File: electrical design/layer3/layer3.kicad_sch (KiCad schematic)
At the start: 6 parts, among them U1 TEENSY4.0

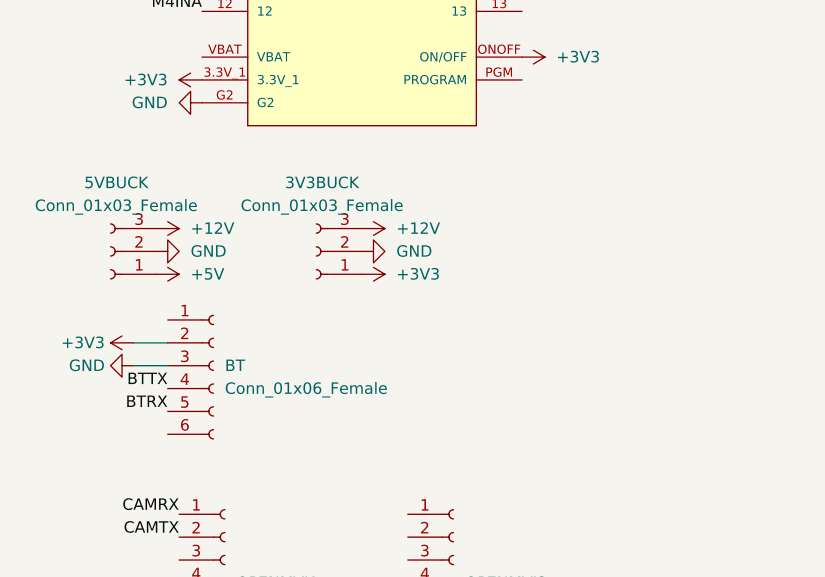
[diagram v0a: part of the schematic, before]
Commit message: add support for bldc esc
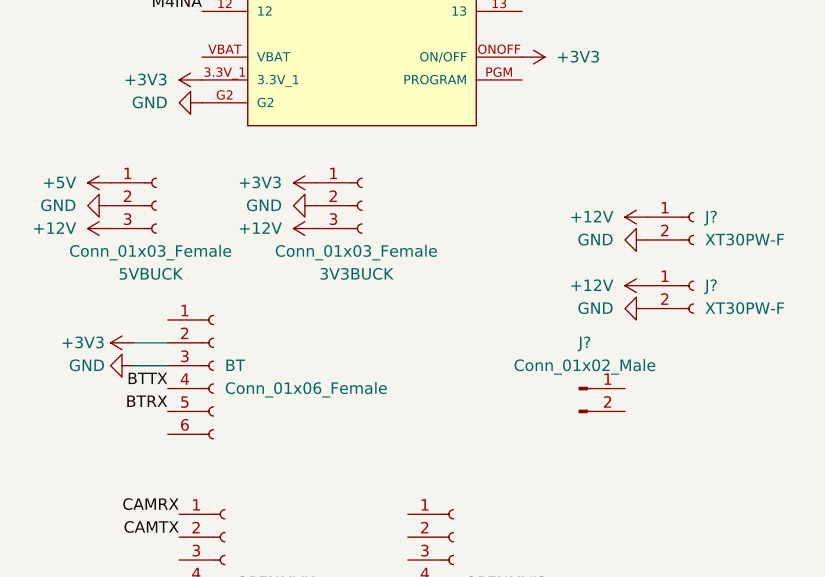
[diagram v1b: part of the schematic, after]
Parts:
- added J?: Conn_01x02_Male, symbol Connector:Conn_01x02_Male
- added J? (x2): XT30PW-F, symbol Connector:Conn_01x02_Female
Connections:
- net +12V: now also J?.1 (Pin_1), J?.1 (Pin_1)
- net GND: now also J?.2 (Pin_2), J?.2 (Pin_2)
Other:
- moved on the sheet: 3V3BUCK, 5VBUCK

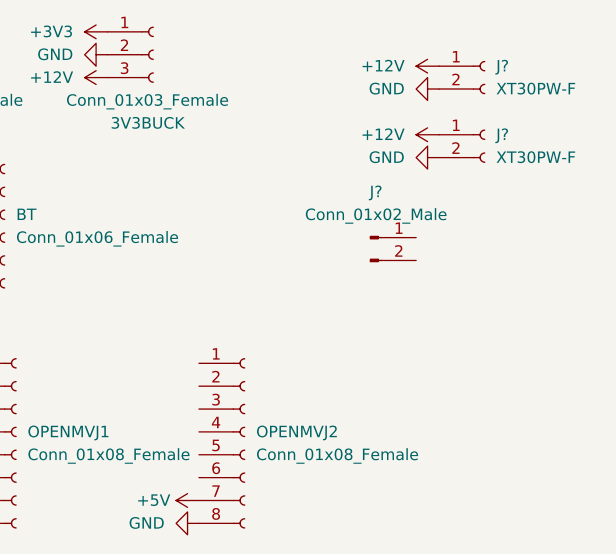
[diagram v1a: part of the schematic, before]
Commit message: fix faulty esc connection
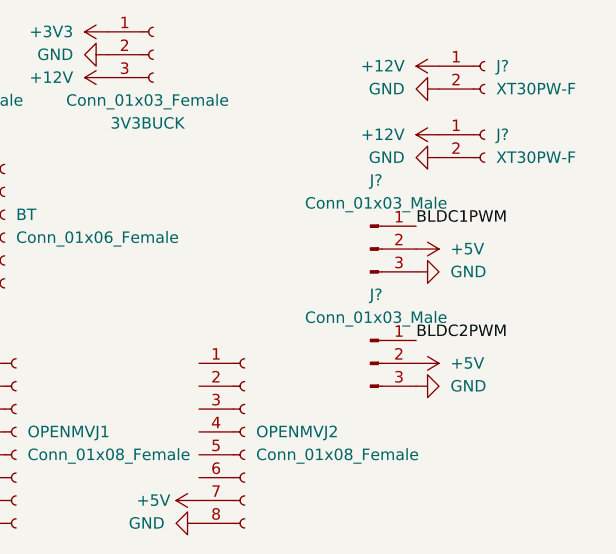
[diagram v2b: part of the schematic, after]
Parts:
- removed J?: Conn_01x02_Male, symbol Connector:Conn_01x02_Male
- added J? (x2): Conn_01x03_Male, symbol Connector:Conn_01x03_Male
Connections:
- net +5V: now also J?.2 (Pin_2), J?.2 (Pin_2)
- net GND: now also J?.3 (Pin_3), J?.3 (Pin_3)
- new net BLDC1PWM: J?.1 (Pin_1)
- new net BLDC2PWM: J?.1 (Pin_1)
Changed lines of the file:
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@@
     (title "layer 3 schematic drawing")
     (date "2022-12-04")
-    (rev "0.2")
+    (rev "0.3")
     (company "8076 Robotics")
   )
@@
     (effects (font (size 1.27 1.27)) (justify left bottom))
   )
+  (label "BLDC2PWM" (at 85.09 114.3 0)
+    (effects (font (size 1.27 1.27)) (justify left bottom))
+  )
   (label "DRIBBLERPWM" (at 38.1 45.72 180)
     (effects (font (size 1.27 1.27)) (justify right bottom))
@@
   (label "M3PWM" (at 38.1 40.64 180)
     (effects (font (size 1.27 1.27)) (justify right bottom))
+  )
+  (label "BLDC1PWM" (at 85.09 101.6 0)
+    (effects (font (size 1.27 1.27)) (justify left bottom))
   )
   (label "M1PWM" (at 38.1 35.56 180)
@@
     (pin "6")
   )
+  (symbol (lib_id "Connector:Conn_01x03_Male") (at 80.01 116.84 0) (unit 1)
+    (in_bom yes) (on_board yes) (fields_autoplaced)
+    (property "Reference" "J?" (id 0) (at 80.645 109.22 0))
+    (property "Value" "Conn_01x03_Male" (id 1) (at 80.645 111.76 0))
+    (property "Footprint" "" (id 2) (at 80.01 116.84 0)
+      (effects (font (size 1.27 1.27)) hide)
+    )
+    (property "Datasheet" "~" (id 3) (at 80.01 116.84 0)
+      (effects (font (size 1.27 1.27)) hide)
+    )
+    (pin "1")
+    (pin "2")
+    (pin "3")
+  )
   (symbol (lib_id "power:+3V3") (at 38.1 68.58 90) (unit 1)
     (in_bom yes) (on_board yes) (fields_autoplaced)
@@
     (pin "1")
   )
-  (symbol (lib_id "Connector:Conn_01x02_Male") (at 80.01 102.87 0) (unit 1)
-    (in_bom yes) (on_board yes) (fields_autoplaced)
-    (property "Reference" "J?" (id 0) (at 80.645 97.79 0))
-    (property "Value" "Conn_01x02_Male" (id 1) (at 80.645 100.33 0))
-    (property "Footprint" "" (id 2) (at 80.01 102.87 0)
-      (effects (font (size 1.27 1.27)) hide)
-    )
-    (property "Datasheet" "~" (id 3) (at 80.01 102.87 0)
-      (effects (font (size 1.27 1.27)) hide)
-    )
-    (pin "1")
-    (pin "2")
+  (symbol (lib_id "power:GND") (at 85.09 106.68 90) (unit 1)
+    (in_bom yes) (on_board yes) (fields_autoplaced)
+    (property "Reference" "#PWR?" (id 0) (at 91.44 106.68 0)
+      (effects (font (size 1.27 1.27)) hide)
+    )
+    (property "Value" "GND" (id 1) (at 88.9 106.6799 90)
+      (effects (font (size 1.27 1.27)) (justify right))
+    )
+    (property "Footprint" "" (id 2) (at 85.09 106.68 0)
+      (effects (font (size 1.27 1.27)) hide)
+    )
+    (property "Datasheet" "" (id 3) (at 85.09 106.68 0)
+      (effects (font (size 1.27 1.27)) hide)
+    )
+    (pin "1")
+  )
+  (symbol (lib_id "power:GND") (at 85.09 119.38 90) (unit 1)
+    (in_bom yes) (on_board yes) (fields_autoplaced)
+    (property "Reference" "#PWR?" (id 0) (at 91.44 119.38 0)
+      (effects (font (size 1.27 1.27)) hide)
+    )
+    (property "Value" "GND" (id 1) (at 88.9 119.3799 90)
+      (effects (font (size 1.27 1.27)) (justify right))
+    )
+    (property "Footprint" "" (id 2) (at 85.09 119.38 0)
+      (effects (font (size 1.27 1.27)) hide)
+    )
+    (property "Datasheet" "" (id 3) (at 85.09 119.38 0)
+      (effects (font (size 1.27 1.27)) hide)
+    )
+    (pin "1")
+  )
+  (symbol (lib_id "power:+5V") (at 85.09 116.84 270) (unit 1)
+    (in_bom yes) (on_board yes) (fields_autoplaced)
+    (property "Reference" "#PWR?" (id 0) (at 81.28 116.84 0)
+      (effects (font (size 1.27 1.27)) hide)
+    )
+    (property "Value" "+5V" (id 1) (at 88.9 116.8399 90)
+      (effects (font (size 1.27 1.27)) (justify left))
+    )
+    (property "Footprint" "" (id 2) (at 85.09 116.84 0)
+      (effects (font (size 1.27 1.27)) hide)
+    )
+    (property "Datasheet" "" (id 3) (at 85.09 116.84 0)
+      (effects (font (size 1.27 1.27)) hide)
+    )
+    (pin "1")
   )
   (symbol (lib_id "power:+12V") (at 87.63 91.44 90) (unit 1)
@@
     (pin "1")
   )
+  (symbol (lib_id "Connector:Conn_01x03_Male") (at 80.01 104.14 0) (unit 1)
+    (in_bom yes) (on_board yes) (fields_autoplaced)
+    (property "Reference" "J?" (id 0) (at 80.645 96.52 0))
+    (property "Value" "Conn_01x03_Male" (id 1) (at 80.645 99.06 0))
+    (property "Footprint" "" (id 2) (at 80.01 104.14 0)
+      (effects (font (size 1.27 1.27)) hide)
+    )
+    (property "Datasheet" "~" (id 3) (at 80.01 104.14 0)
+      (effects (font (size 1.27 1.27)) hide)
+    )
+    (pin "1")
+    (pin "2")
+    (pin "3")
+  )
   (symbol (lib_id "power:GND") (at 38.1 27.94 270) (unit 1)
     (in_bom yes) (on_board yes) (fields_autoplaced)
@@
     )
     (property "Datasheet" "" (id 3) (at 73.66 30.48 0)
+      (effects (font (size 1.27 1.27)) hide)
+    )
+    (pin "1")
+  )
+  (symbol (lib_id "power:+5V") (at 85.09 104.14 270) (unit 1)
+    (in_bom yes) (on_board yes) (fields_autoplaced)
+    (property "Reference" "#PWR?" (id 0) (at 81.28 104.14 0)
+      (effects (font (size 1.27 1.27)) hide)
+    )
+    (property "Value" "+5V" (id 1) (at 88.9 104.1399 90)
+      (effects (font (size 1.27 1.27)) (justify left))
+    )
+    (property "Footprint" "" (id 2) (at 85.09 104.14 0)
+      (effects (font (size 1.27 1.27)) hide)
+    )
+    (property "Datasheet" "" (id 3) (at 85.09 104.14 0)
       (effects (font (size 1.27 1.27)) hide)
     )
@@
       (reference "#PWR?") (unit 1) (value "+3V3") (footprint "")
     )
+    (path "/1c20d470-dfbb-44ac-bcd7-6f44788a3215"
+      (reference "#PWR?") (unit 1) (value "GND") (footprint "")
+    )
+    (path "/1f303e68-81aa-42e0-b038-4ed10640f13e"
+      (reference "#PWR?") (unit 1) (value "GND") (footprint "")
+    )
+    (path "/2600c1a9-fa17-45e3-9c4a-d07aecf1ab7b"
+      (reference "#PWR?") (unit 1) (value "+5V") (footprint "")
+    )
     (path "/31a53b3b-6cac-4aca-8532-f8abd9adb007"
       (reference "#PWR?") (unit 1) (value "+12V") (footprint "")
@@
       (reference "#PWR?") (unit 1) (value "GND") (footprint "")
     )
+    (path "/62071202-a64d-4696-9e70-81f99028e10f"
+      (reference "#PWR?") (unit 1) (value "+5V") (footprint "")
+    )
     (path "/65f12a69-4b30-4824-8542-8c0ea2d496b2"
       (reference "#PWR?") (unit 1) (value "GND") (footprint "")
@@
       (reference "BT") (unit 1) (value "Conn_01x06_Female") (footprint "")
     )
-    (path "/235b7ba9-f780-4097-9ee6-104a623911c8"
-      (reference "J?") (unit 1) (value "Conn_01x02_Male") (footprint "")
+    (path "/0605672f-fcfa-45e6-9f4e-33c2774354d0"
+      (reference "J?") (unit 1) (value "Conn_01x03_Male") (footprint "")
+    )
+    (path "/4084b486-2699-4f5c-85d5-b7cc2be63b6e"
+      (reference "J?") (unit 1) (value "Conn_01x03_Male") (footprint "")
     )
     (path "/6cb35fab-0b3b-49d8-a75d-48e6927a426a"

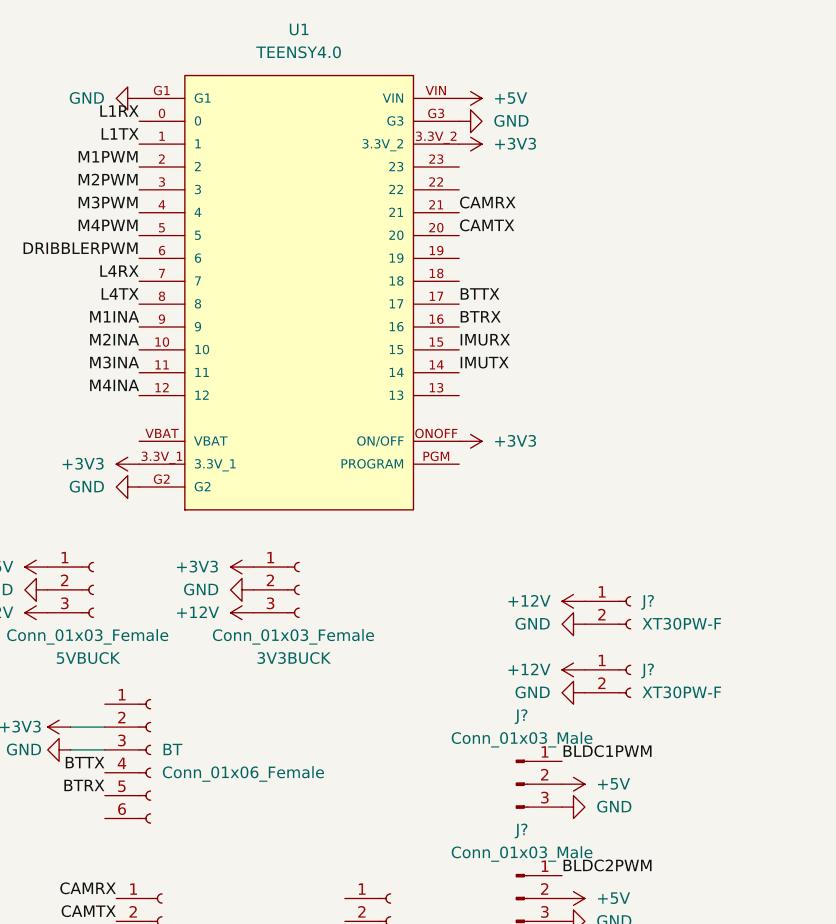
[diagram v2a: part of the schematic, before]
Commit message: update layer 1 and 3 schematics
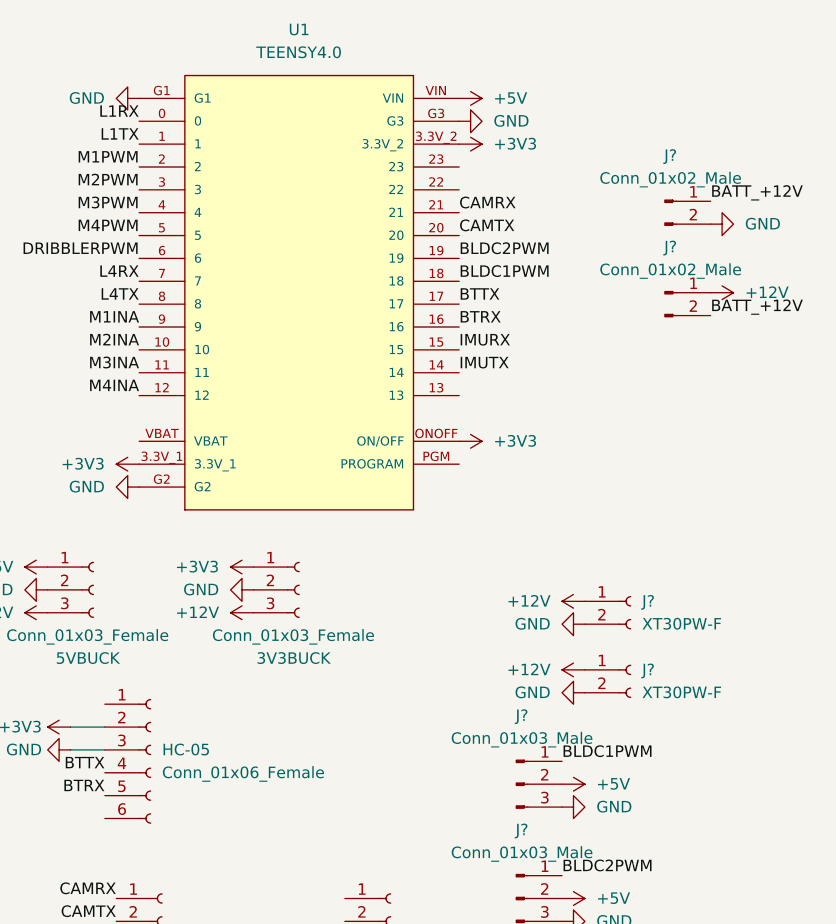
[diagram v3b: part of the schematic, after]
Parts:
- added J? (x2): Conn_01x02_Male, symbol Connector:Conn_01x02_Male
- renumbered BT to HC-05
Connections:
- net +12V: now also J?.1 (Pin_1)
- net BLDC1PWM: now also U1.18
- net BLDC2PWM: now also U1.19
- net GND: now also J?.2 (Pin_2)
- new net BATT_+12V: J?.1 (Pin_1), J?.2 (Pin_2)
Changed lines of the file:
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@@
     (effects (font (size 1.27 1.27)) (justify right bottom))
+  )
+  (label "BLDC1PWM" (at 73.66 48.26 0)
+    (effects (font (size 1.27 1.27)) (justify left bottom))
   )
   (label "CAMTX" (at 73.66 43.18 0)
     (effects (font (size 1.27 1.27)) (justify left bottom))
   )
+  (label "BATT_+12V" (at 101.6 39.37 0)
+    (effects (font (size 1.27 1.27)) (justify left bottom))
+  )
   (label "CAMTX" (at 35.56 119.38 180)
     (effects (font (size 1.27 1.27)) (justify right bottom))
@@
     (effects (font (size 1.27 1.27)) (justify right bottom))
   )
+  (label "BLDC2PWM" (at 73.66 45.72 0)
+    (effects (font (size 1.27 1.27)) (justify left bottom))
+  )
   (label "M2PWM" (at 38.1 38.1 180)
     (effects (font (size 1.27 1.27)) (justify right bottom))
@@
     (effects (font (size 1.27 1.27)) (justify left bottom))
   )
+  (label "BATT_+12V" (at 101.6 52.07 0)
+    (effects (font (size 1.27 1.27)) (justify left bottom))
+  )
   (symbol (lib_id "Connector:Conn_01x06_Female") (at 39.37 100.33 0) (unit 1)
     (in_bom yes) (on_board yes) (fields_autoplaced)
-    (property "Reference" "BT" (id 0) (at 40.64 100.3299 0)
+    (property "Reference" "HC-05" (id 0) (at 40.64 100.3299 0)
       (effects (font (size 1.27 1.27)) (justify left))
     )
@@
     (pin "3")
   )
+  (symbol (lib_id "power:GND") (at 101.6 41.91 90) (unit 1)
+    (in_bom yes) (on_board yes) (fields_autoplaced)
+    (property "Reference" "#PWR?" (id 0) (at 107.95 41.91 0)
+      (effects (font (size 1.27 1.27)) hide)
+    )
+    (property "Value" "GND" (id 1) (at 105.41 41.9099 90)
+      (effects (font (size 1.27 1.27)) (justify right))
+    )
+    (property "Footprint" "" (id 2) (at 101.6 41.91 0)
+      (effects (font (size 1.27 1.27)) hide)
+    )
+    (property "Datasheet" "" (id 3) (at 101.6 41.91 0)
+      (effects (font (size 1.27 1.27)) hide)
+    )
+    (pin "1")
+  )
   (symbol (lib_id "power:+3V3") (at 38.1 68.58 90) (unit 1)
     (in_bom yes) (on_board yes) (fields_autoplaced)
@@
     )
     (pin "1")
+  )
+  (symbol (lib_id "Connector:Conn_01x02_Male") (at 96.52 49.53 0) (unit 1)
+    (in_bom yes) (on_board yes) (fields_autoplaced)
+    (property "Reference" "J?" (id 0) (at 97.155 44.45 0))
+    (property "Value" "Conn_01x02_Male" (id 1) (at 97.155 46.99 0))
+    (property "Footprint" "" (id 2) (at 96.52 49.53 0)
+      (effects (font (size 1.27 1.27)) hide)
+    )
+    (property "Datasheet" "~" (id 3) (at 96.52 49.53 0)
+      (effects (font (size 1.27 1.27)) hide)
+    )
+    (pin "1")
+    (pin "2")
   )
   (symbol (lib_id "power:+5V") (at 85.09 104.14 270) (unit 1)
@@
     (pin "1")
   )
+  (symbol (lib_id "power:+12V") (at 101.6 49.53 270) (unit 1)
+    (in_bom yes) (on_board yes) (fields_autoplaced)
+    (property "Reference" "#PWR?" (id 0) (at 97.79 49.53 0)
+      (effects (font (size 1.27 1.27)) hide)
+    )
+    (property "Value" "+12V" (id 1) (at 105.41 49.5299 90)
+      (effects (font (size 1.27 1.27)) (justify left))
+    )
+    (property "Footprint" "" (id 2) (at 101.6 49.53 0)
+      (effects (font (size 1.27 1.27)) hide)
+    )
+    (property "Datasheet" "" (id 3) (at 101.6 49.53 0)
+      (effects (font (size 1.27 1.27)) hide)
+    )
+    (pin "1")
+  )
   (symbol (lib_id "power:GND") (at 60.96 134.62 270) (unit 1)
     (in_bom yes) (on_board yes) (fields_autoplaced)
@@
     (pin "8")
   )
+  (symbol (lib_id "Connector:Conn_01x02_Male") (at 96.52 39.37 0) (unit 1)
+    (in_bom yes) (on_board yes) (fields_autoplaced)
+    (property "Reference" "J?" (id 0) (at 97.155 34.29 0))
+    (property "Value" "Conn_01x02_Male" (id 1) (at 97.155 36.83 0))
+    (property "Footprint" "" (id 2) (at 96.52 39.37 0)
+      (effects (font (size 1.27 1.27)) hide)
+    )
+    (property "Datasheet" "~" (id 3) (at 96.52 39.37 0)
+      (effects (font (size 1.27 1.27)) hide)
+    )
+    (pin "1")
+    (pin "2")
+  )
   (symbol (lib_id "power:GND") (at 87.63 93.98 270) (unit 1)
     (in_bom yes) (on_board yes) (fields_autoplaced)
@@
   )
   (symbol_instances
+    (path "/0c89ad61-56a3-4409-b4d9-3241797b2bba"
+      (reference "#PWR?") (unit 1) (value "GND") (footprint "")
+    )
     (path "/0ece3660-c0d6-451d-ab90-452a064e25d5"
       (reference "#PWR?") (unit 1) (value "+3V3") (footprint "")
@@
       (reference "#PWR?") (unit 1) (value "GND") (footprint "")
     )
+    (path "/80fd3eb9-7ad4-41f8-a7f1-19ecc30e10a7"
+      (reference "#PWR?") (unit 1) (value "+12V") (footprint "")
+    )
     (path "/b69e7d5c-78f5-4f1c-a2dc-b63c367fcd30"
       (reference "#PWR?") (unit 1) (value "GND") (footprint "")
@@
     )
     (path "/05568742-0152-4de6-b990-21dd9f504cc9"
-      (reference "BT") (unit 1) (value "Conn_01x06_Female") (footprint "")
+      (reference "HC-05") (unit 1) (value "Conn_01x06_Female") (footprint "")
     )
     (path "/0605672f-fcfa-45e6-9f4e-33c2774354d0"
@@
       (reference "J?") (unit 1) (value "Conn_01x03_Male") (footprint "")
     )
+    (path "/5f51e85d-3704-4d50-8831-e2277ef10216"
+      (reference "J?") (unit 1) (value "Conn_01x02_Male") (footprint "")
+    )
     (path "/6cb35fab-0b3b-49d8-a75d-48e6927a426a"
       (reference "J?") (unit 1) (value "XT30PW-F") (footprint "")
     )
+    (path "/becd3c5c-112e-42c6-8efc-4cd7f4b52ecb"
+      (reference "J?") (unit 1) (value "Conn_01x02_Male") (footprint "")
+    )
     (path "/d9b4a0a0-024d-42f7-878a-1562f6b83722"

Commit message: update layer 1 and layer 3 pcbs
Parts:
- removed J?: Conn_01x03_Male, symbol Connector:Conn_01x03_Male
- removed OPENMVJ1, OPENMVJ2: Conn_01x08_Female, Connectors:1X08_FEMALE_LOCK, symbol Connector:Conn_01x08_Female
- added LIDAR1: XH2.54 5P, symbol Connector:Conn_01x05_Male
- BUCK1: renamed from 5VBUCK; value Conn_01x03_Female -> +5V
- BUCK2: renamed from 3V3BUCK; value Conn_01x03_Female -> +3V3
- J? (x2): value Conn_01x02_Male -> XT60PW-M
- U1: value TEENSY4.0 -> TEENSY 4.0
- renumbered HC-05 to BT1
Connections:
- net BLDC1PWM is gone; now on net DRIBBLERPWM: J?.1 (Pin_1), U1.18
- net +5V: now also LIDAR1.1 (Pin_1)
- net GND: now also LIDAR1.4 (Pin_4)
- net BLDC2PWM: no longer names the net of U1.19
- new net LIDARRX: LIDAR1.3 (Pin_3)
- new net LIDARTX: LIDAR1.2 (Pin_2)
- new net MOTOCT: LIDAR1.5 (Pin_5)
